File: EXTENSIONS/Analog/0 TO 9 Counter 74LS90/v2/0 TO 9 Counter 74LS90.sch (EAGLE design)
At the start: 22 parts

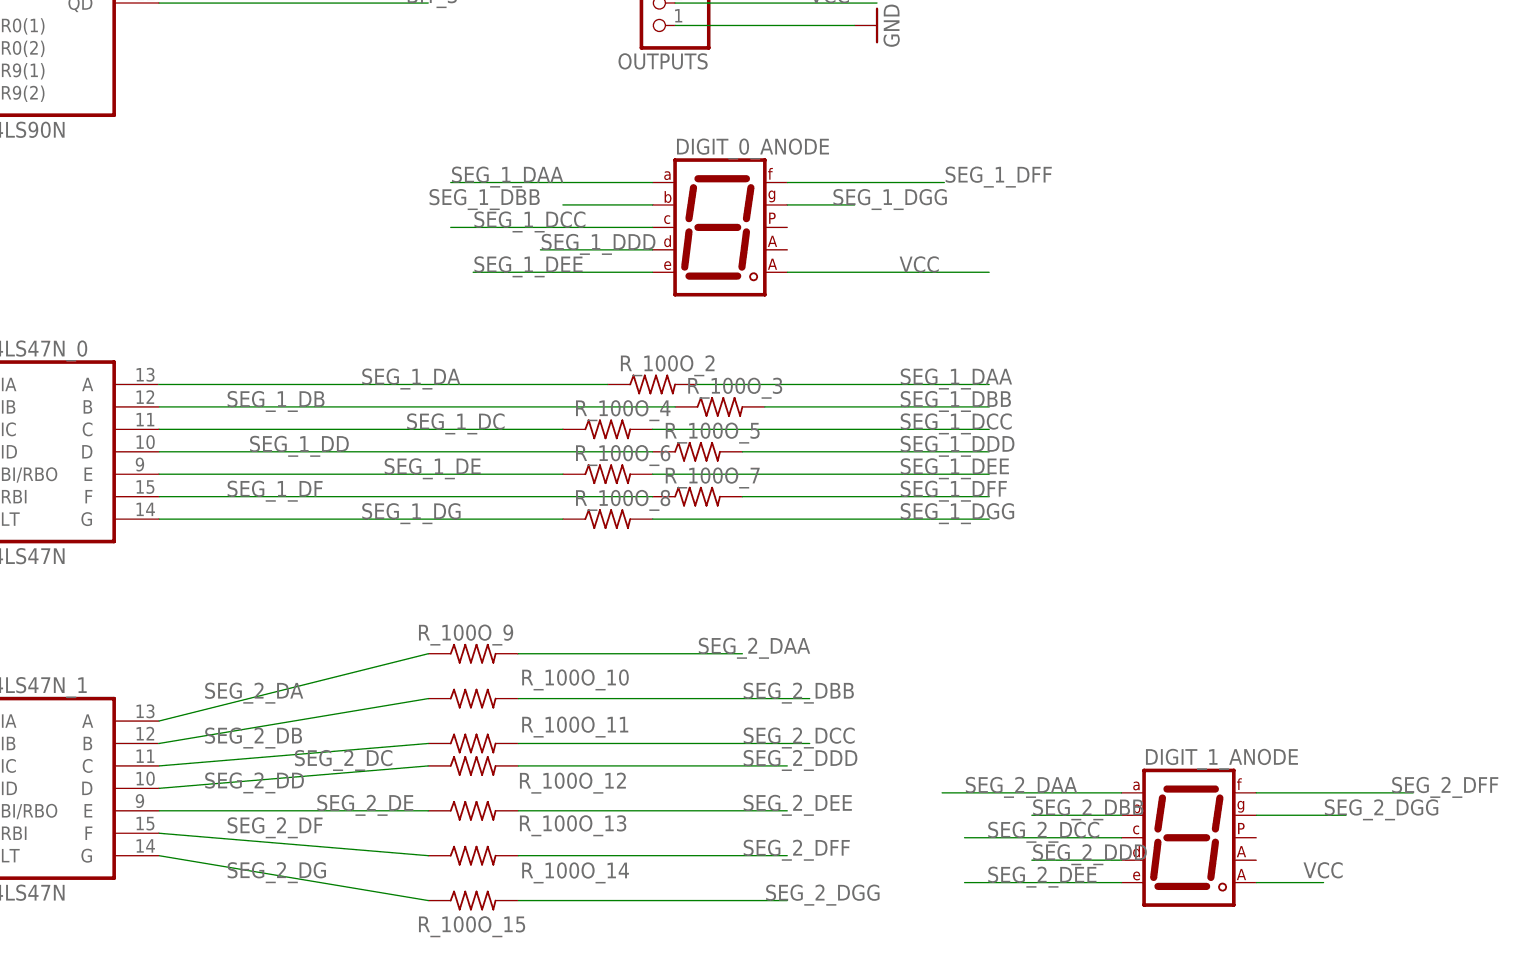
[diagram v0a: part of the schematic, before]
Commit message: Create v3 of 0 to 99 counter
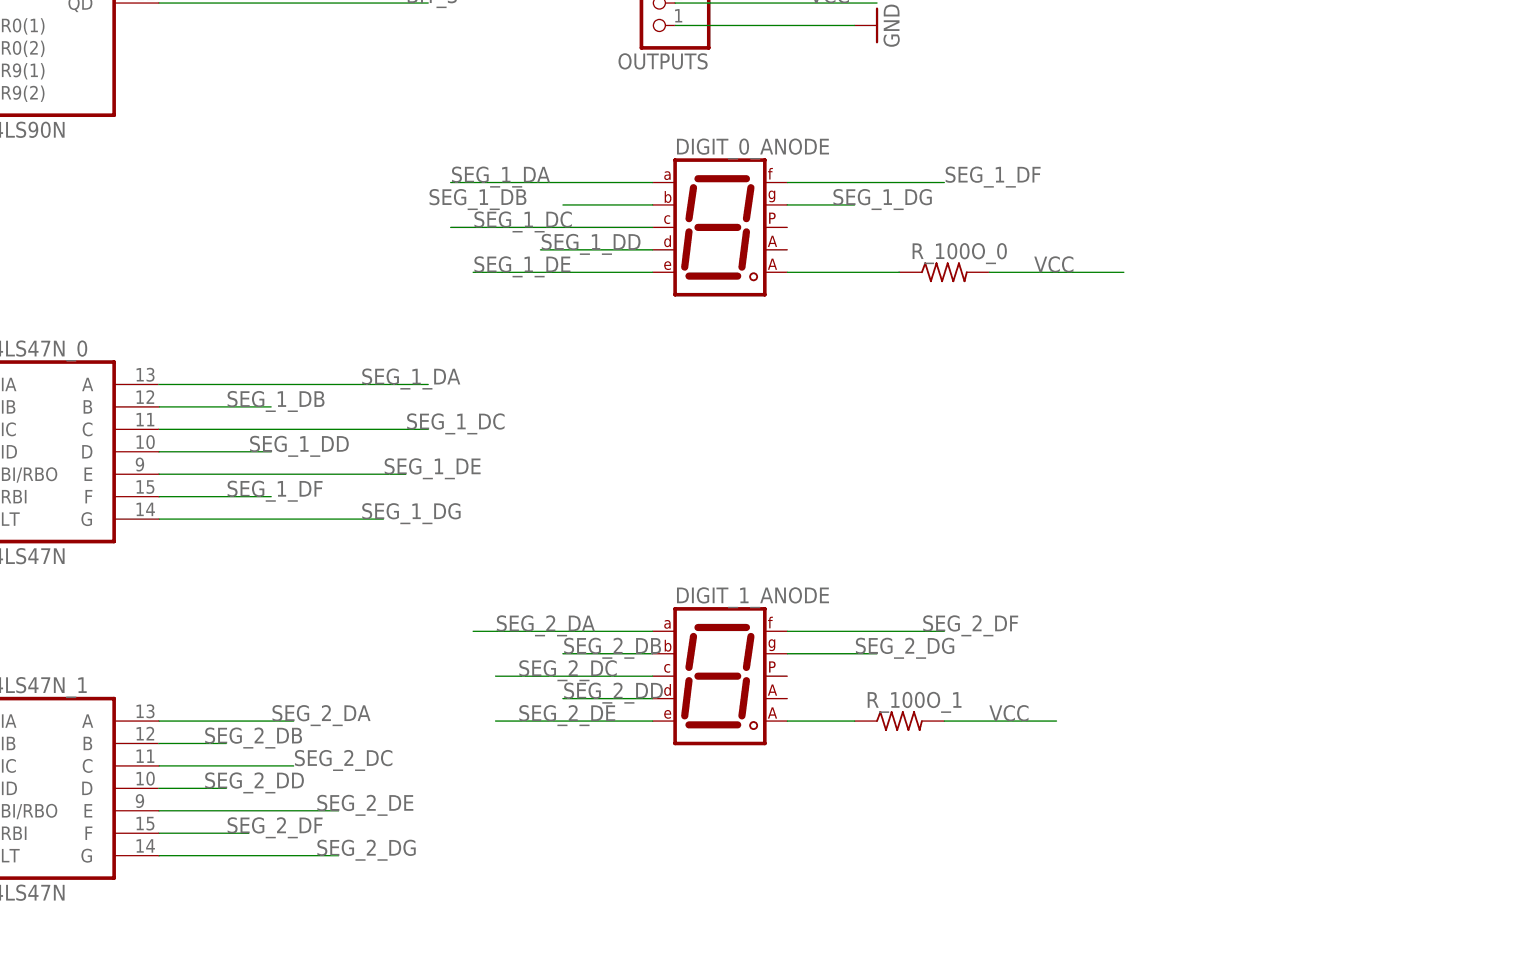
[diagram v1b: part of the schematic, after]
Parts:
- removed R_100O_10, R_100O_11, R_100O_12, R_100O_13, R_100O_14, R_100O_15, R_100O_2, R_100O_3, R_100O_4, R_100O_5, R_100O_6, R_100O_7, R_100O_8, R_100O_9: (no value), adafruit:R-US_R1206
- added R_100O_0, R_100O_1: (no value), adafruit:R-US_R1206
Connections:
- removed net SEG_1_DAA: DIGIT_0_ANODE.A, R_100O_2.2
- removed net SEG_1_DBB: DIGIT_0_ANODE.B, R_100O_3.2
- removed net SEG_1_DCC: DIGIT_0_ANODE.C, R_100O_4.2
- removed net SEG_1_DDD: DIGIT_0_ANODE.D, R_100O_5.2
- removed net SEG_1_DEE: DIGIT_0_ANODE.E, R_100O_6.2
- removed net SEG_1_DFF: DIGIT_0_ANODE.F, R_100O_7.2
- removed net SEG_1_DGG: DIGIT_0_ANODE.G, R_100O_8.2
- removed net SEG_2_DAA: DIGIT_1_ANODE.A, R_100O_9.2
- removed net SEG_2_DBB: DIGIT_1_ANODE.B, R_100O_10.2
- removed net SEG_2_DCC: DIGIT_1_ANODE.C, R_100O_11.2
- removed net SEG_2_DDD: DIGIT_1_ANODE.D, R_100O_12.2
- removed net SEG_2_DEE: DIGIT_1_ANODE.E, R_100O_13.2
- removed net SEG_2_DFF: DIGIT_1_ANODE.F, R_100O_14.2
- removed net SEG_2_DGG: DIGIT_1_ANODE.G, R_100O_15.2
- new net N$1: DIGIT_0_ANODE.CA2, R_100O_0.1
- new net N$2: DIGIT_1_ANODE.CA2, R_100O_1.1
- net SEG_1_DA: now also DIGIT_0_ANODE.A; no longer R_100O_2.1
- net SEG_1_DB: now also DIGIT_0_ANODE.B; no longer R_100O_3.1
- net SEG_1_DC: now also DIGIT_0_ANODE.C; no longer R_100O_4.1
- net SEG_1_DD: now also DIGIT_0_ANODE.D; no longer R_100O_5.1
- net SEG_1_DE: now also DIGIT_0_ANODE.E; no longer R_100O_6.1
- net SEG_1_DF: now also DIGIT_0_ANODE.F; no longer R_100O_7.1
- net SEG_1_DG: now also DIGIT_0_ANODE.G; no longer R_100O_8.1
- net SEG_2_DA: now also DIGIT_1_ANODE.A; no longer R_100O_9.1
- net SEG_2_DB: now also DIGIT_1_ANODE.B; no longer R_100O_10.1
- net SEG_2_DC: now also DIGIT_1_ANODE.C; no longer R_100O_11.1
- net SEG_2_DD: now also DIGIT_1_ANODE.D; no longer R_100O_12.1
- net SEG_2_DE: now also DIGIT_1_ANODE.E; no longer R_100O_13.1
- net SEG_2_DF: now also DIGIT_1_ANODE.F; no longer R_100O_14.1
- net SEG_2_DG: now also DIGIT_1_ANODE.G; no longer R_100O_15.1
- net VCC: now also R_100O_0.2, R_100O_1.2; no longer DIGIT_0_ANODE.CA2, DIGIT_1_ANODE.CA2
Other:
- moved on the sheet: DIGIT_1_ANODE
